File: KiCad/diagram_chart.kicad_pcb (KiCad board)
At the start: 2 copper layers, 120 x 120 mm, 115 parts, among them SW0 SW0, SW1 SW1, SW2 SW2, SW3 SW3, SW4 SW4, SW5 SW5, SW6 SW6, SW7 SW7, U1 TPIC6C595, U2 74HC165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

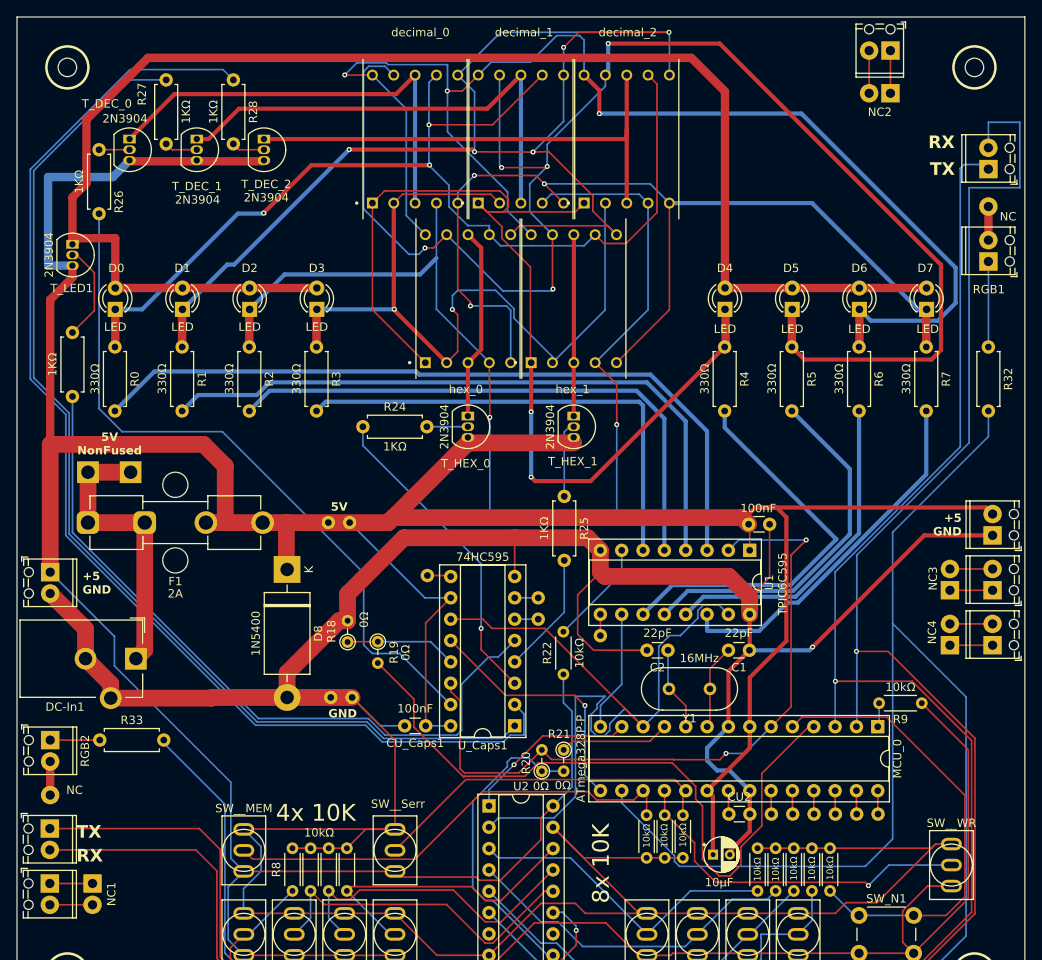
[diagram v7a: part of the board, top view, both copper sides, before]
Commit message: Removed holes from terminal-screws. Obs the gerber files here are not the ones ordered. I will upload zip from pcbway in next commit.
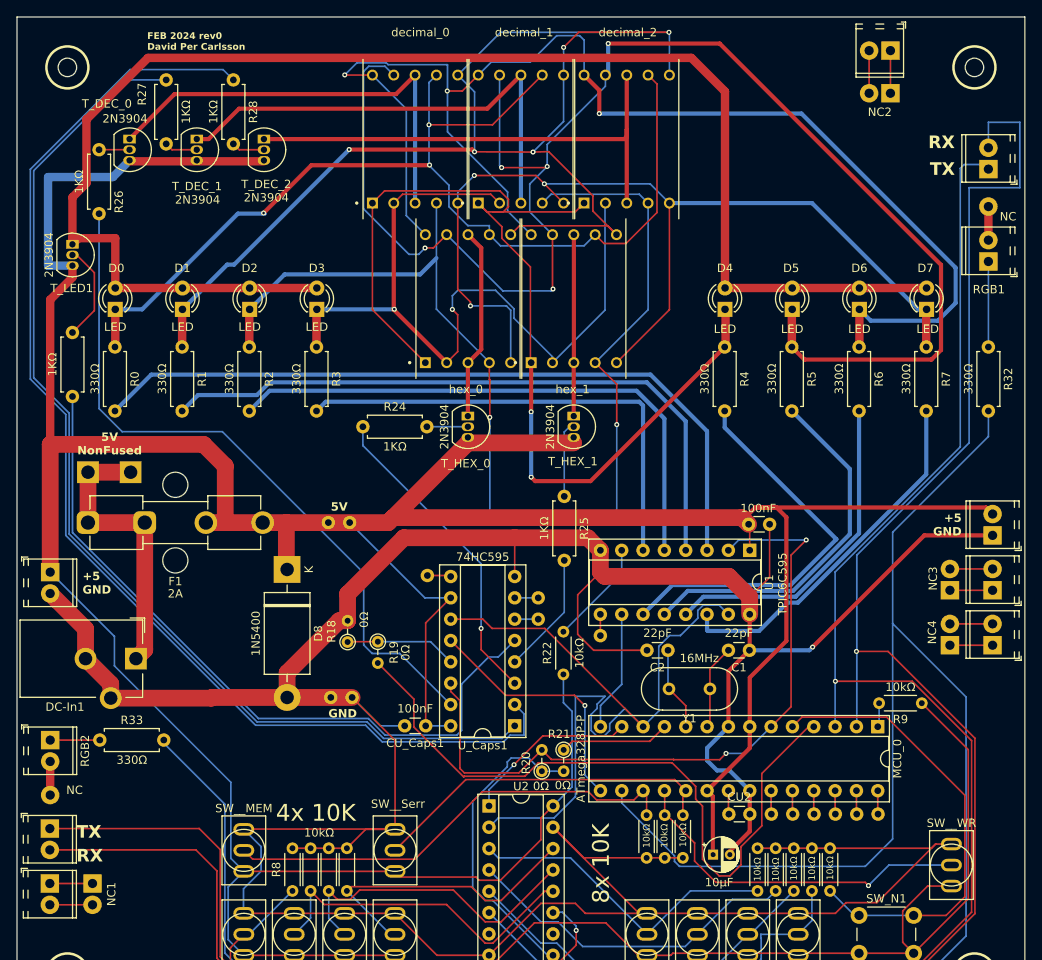
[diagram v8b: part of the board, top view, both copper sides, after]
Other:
- board text added: "FEB 2024 rev0 David Per Carlsson"
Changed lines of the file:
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@@
       (outputformat 1)
       (mirror false)
-      (drillshape 1)
+      (drillshape 0)
       (scaleselection 1)
       (outputdirectory "")
@@
         (effects (font (size 1 1) (thickness 0.15)))
     )
+    (fp_text user "${REFERENCE}" (at 1.27 2 90) (layer "F.Fab")
+        (effects (font (size 1 1) (thickness 0.15)))
+    )
     (fp_line (start -1.8 2.66) (end -1.8 3.4)
       (stroke (width 0.12) (type solid)) (layer "F.SilkS"))
@@
     (fp_circle (center 2.54 0) (end 3.64 0)
       (stroke (width 0.1) (type solid)) (fill none) (layer "F.Fab"))
-    (pad "" np_thru_hole circle (at 0 2.54 90) (size 1.1 1.1) (drill 1.1) (layers "*.Cu" "*.Mask"))
-    (pad "" np_thru_hole circle (at 2.54 2.54 90) (size 1.1 1.1) (drill 1.1) (layers "*.Cu" "*.Mask"))
     (pad "1" thru_hole rect (at 0 0 90) (size 2.2 2.2) (drill 1.1) (layers "*.Cu" "*.Mask")
       (net 78 "Net-(MCU_0-PD1)") (pinfunction "Pin_1") (pintype "passive"))
@@
         (effects (font (size 1 1) (thickness 0.15)))
     )
+    (fp_text user "${REFERENCE}" (at 1.27 2 90) (layer "F.Fab")
+        (effects (font (size 1 1) (thickness 0.15)))
+    )
     (fp_line (start -1.8 2.66) (end -1.8 3.4)
       (stroke (width 0.12) (type solid)) (layer "F.SilkS"))
@@
     (fp_circle (center 2.54 0) (end 3.64 0)
       (stroke (width 0.1) (type solid)) (fill none) (layer "F.Fab"))
-    (pad "" np_thru_hole circle (at 0 2.54 90) (size 1.1 1.1) (drill 1.1) (layers "*.Cu" "*.Mask"))
-    (pad "" np_thru_hole circle (at 2.54 2.54 90) (size 1.1 1.1) (drill 1.1) (layers "*.Cu" "*.Mask"))
     (pad "1" thru_hole rect (at 0 0 90) (size 2.2 2.2) (drill 1.1) (layers "*.Cu" "*.Mask")
       (net 1 "GND") (pinfunction "Pin_1") (pintype "passive"))
@@
         (effects (font (size 1 1) (thickness 0.15)))
     )
+    (fp_text user "${REFERENCE}" (at 1.27 2 -90) (layer "F.Fab")
+        (effects (font (size 1 1) (thickness 0.15)))
+    )
     (fp_line (start -1.8 2.66) (end -1.8 3.4)
       (stroke (width 0.12) (type solid)) (layer "F.SilkS"))
@@
     (fp_circle (center 2.54 0) (end 3.64 0)
       (stroke (width 0.1) (type solid)) (fill none) (layer "F.Fab"))
-    (pad "" np_thru_hole circle (at 0 2.54 270) (size 1.1 1.1) (drill 1.1) (layers "*.Cu" "*.Mask"))
-    (pad "" np_thru_hole circle (at 2.54 2.54 270) (size 1.1 1.1) (drill 1.1) (layers "*.Cu" "*.Mask"))
     (pad "1" thru_hole rect (at 0 0 270) (size 2.2 2.2) (drill 1.1) (layers "*.Cu" "*.Mask")
       (net 78 "Net-(MCU_0-PD1)") (pinfunction "Pin_1") (pintype "passive"))
@@
     (fp_circle (center 2.54 0) (end 3.64 0)
       (stroke (width 0.1) (type solid)) (fill none) (layer "F.Fab"))
-    (pad "" np_thru_hole circle (at 0 2.54 90) (size 1.1 1.1) (drill 1.1) (layers "*.Cu" "*.Mask"))
-    (pad "" np_thru_hole circle (at 2.54 2.54 90) (size 1.1 1.1) (drill 1.1) (layers "*.Cu" "*.Mask"))
     (pad "1" thru_hole rect (at 0 0 90) (size 2.2 2.2) (drill 1.1) (layers "*.Cu" "*.Mask")
       (net 89 "unconnected-(NC4-Pin_1-Pad1)") (pinfunction "Pin_1") (pintype "passive"))
@@
     (fp_circle (center 2.54 0) (end 3.64 0)
       (stroke (width 0.1) (type solid)) (fill none) (layer "F.Fab"))
-    (pad "" np_thru_hole circle (at 0 2.54 90) (size 1.1 1.1) (drill 1.1) (layers "*.Cu" "*.Mask"))
-    (pad "" np_thru_hole circle (at 2.54 2.54 90) (size 1.1 1.1) (drill 1.1) (layers "*.Cu" "*.Mask"))
     (pad "1" thru_hole rect (at 0 0 90) (size 2.2 2.2) (drill 1.1) (layers "*.Cu" "*.Mask")
       (net 87 "unconnected-(NC3-Pin_1-Pad1)") (pinfunction "Pin_1") (pintype "passive"))
@@
     (fp_circle (center 2.54 0) (end 3.64 0)
       (stroke (width 0.1) (type solid)) (fill none) (layer "F.Fab"))
-    (pad "" np_thru_hole circle (at 0 2.54 270) (size 1.1 1.1) (drill 1.1) (layers "*.Cu" "*.Mask"))
-    (pad "" np_thru_hole circle (at 2.54 2.54 270) (size 1.1 1.1) (drill 1.1) (layers "*.Cu" "*.Mask"))
     (pad "1" thru_hole rect (at 0 0 270) (size 2.2 2.2) (drill 1.1) (layers "*.Cu" "*.Mask")
       (net 83 "unconnected-(NC1-Pin_1-Pad1)") (pinfunction "Pin_1") (pintype "passive"))
@@
         (effects (font (size 1 1) (thickness 0.15)))
     )
-    (fp_text value "330Ω" (at 3.81 2.37 90) (layer "F.Fab")
+    (fp_text value "330Ω" (at 3.81 2.37 90) (layer "F.SilkS")
         (effects (font (size 1 1) (thickness 0.15)))
     )
@@
     (fp_circle (center 2.54 0) (end 3.64 0)
       (stroke (width 0.1) (type solid)) (fill none) (layer "F.Fab"))
-    (pad "" np_thru_hole circle (at 0 2.54 180) (size 1.1 1.1) (drill 1.1) (layers "*.Cu" "*.Mask"))
-    (pad "" np_thru_hole circle (at 2.54 2.54 180) (size 1.1 1.1) (drill 1.1) (layers "*.Cu" "*.Mask"))
     (pad "1" thru_hole rect (at 0 0 180) (size 2.2 2.2) (drill 1.1) (layers "*.Cu" "*.Mask")
       (net 85 "unconnected-(NC2-Pin_1-Pad1)") (pinfunction "Pin_1") (pintype "passive"))
@@
         (effects (font (size 1 1) (thickness 0.15)))
     )
-    (fp_text value "330Ω" (at 3.81 2.37) (layer "F.Fab")
+    (fp_text value "330Ω" (at 3.81 2.37) (layer "F.SilkS")
         (effects (font (size 1 1) (thickness 0.15)))
     )
@@
         (effects (font (size 1 1) (thickness 0.15)))
     )
+    (fp_text user "${REFERENCE}" (at 1.27 2 90) (layer "F.Fab")
+        (effects (font (size 1 1) (thickness 0.15)))
+    )
     (fp_line (start -1.8 2.66) (end -1.8 3.4)
       (stroke (width 0.12) (type solid)) (layer "F.SilkS"))
@@
     (fp_circle (center 2.54 0) (end 3.64 0)
       (stroke (width 0.1) (type solid)) (fill none) (layer "F.Fab"))
-    (pad "" np_thru_hole circle (at 0 2.54 90) (size 1.1 1.1) (drill 1.1) (layers "*.Cu" "*.Mask"))
-    (pad "" np_thru_hole circle (at 2.54 2.54 90) (size 1.1 1.1) (drill 1.1) (layers "*.Cu" "*.Mask"))
     (pad "1" thru_hole rect (at 0 0 90) (size 2.2 2.2) (drill 1.1) (layers "*.Cu" "*.Mask")
       (net 80 "Net-(RGB1-Pin_1)") (pinfunction "Pin_1") (pintype "passive"))
@@
     (fp_circle (center 2.54 0) (end 3.64 0)
       (stroke (width 0.1) (type solid)) (fill none) (layer "F.Fab"))
-    (pad "" np_thru_hole circle (at 0 2.54 270) (size 1.1 1.1) (drill 1.1) (layers "*.Cu" "*.Mask"))
-    (pad "" np_thru_hole circle (at 2.54 2.54 270) (size 1.1 1.1) (drill 1.1) (layers "*.Cu" "*.Mask"))
     (pad "1" thru_hole rect (at 0 0 270) (size 2.2 2.2) (drill 1.1) (layers "*.Cu" "*.Mask")
       (net 81 "Net-(RGB2-Pin_1)") (pinfunction "Pin_1") (pintype "passive"))
@@
         (effects (font (size 1 1) (thickness 0.15)))
     )
+    (fp_text user "${REFERENCE}" (at 1.27 2 -90) (layer "F.Fab")
+        (effects (font (size 1 1) (thickness 0.15)))
+    )
     (fp_line (start -1.8 2.66) (end -1.8 3.4)
       (stroke (width 0.12) (type solid)) (layer "F.SilkS"))
@@
     (fp_circle (center 2.54 0) (end 3.64 0)
       (stroke (width 0.1) (type solid)) (fill none) (layer "F.Fab"))
-    (pad "" np_thru_hole circle (at 0 2.54 270) (size 1.1 1.1) (drill 1.1) (layers "*.Cu" "*.Mask"))
-    (pad "" np_thru_hole circle (at 2.54 2.54 270) (size 1.1 1.1) (drill 1.1) (layers "*.Cu" "*.Mask"))
     (pad "1" thru_hole rect (at 0 0 270) (size 2.2 2.2) (drill 1.1) (layers "*.Cu" "*.Mask")
       (net 4 "Net-(D8-K)") (pinfunction "Pin_1") (pintype "passive"))
@@
     (effects (font (size 2 2) (thickness 0.3)) (justify left bottom))
   )
+  (gr_text "FEB 2024 rev0 \nDavid Per Carlsson" (at 66.14 57.3) (layer "F.SilkS")
+    (effects (font (size 0.8 0.8) (thickness 0.15) bold) (justify left bottom))
+  )
   (gr_text "5V" (at 88 112.2) (layer "F.SilkS")
     (effects (font (size 1 1) (thickness 0.25) bold) (justify left bottom))
@@
   (segment (start 153.13 145.42) (end 153.13 148.177) (width 0.2) (layer "F.Cu") (net 38))
   (segment (start 133.13 117.13) (end 132.8 116.8) (width 0.5) (layer "F.Cu") (net 39))
-  (segment (start 98.531 95.88) (end 126.07 95.88) (width 0.5) (layer "B.Cu") (net 39))
   (segment (start 132.8 102.61) (end 132.8 116.8) (width 0.5) (layer "B.Cu") (net 39))
+  (segment (start 62.3 100.21) (end 66.63 95.88) (width 0.5) (layer "B.Cu") (net 39))
   (segment (start 126.07 95.88) (end 132.8 102.61) (width 0.5) (layer "B.Cu") (net 39))
-  (segment (start 98.156 95.505) (end 98.531 95.88) (width 0.5) (layer "B.Cu") (net 39))
-  (segment (start 62.3 100.21) (end 67.005 95.505) (width 0.5) (layer "B.Cu") (net 39))
-  (segment (start 67.005 95.505) (end 98.156 95.505) (width 0.5) (layer "B.Cu") (net 39))
+  (segment (start 66.63 95.88) (end 126.07 95.88) (width 0.5) (layer "B.Cu") (net 39))
   (segment (start 72.2 98.31) (end 79.21005 98.31) (width 0.5) (layer "B.Cu") (net 40))
   (segment (start 70.3 100.21) (end 72.2 98.31) (width 0.5) (layer "B.Cu") (net 40))
